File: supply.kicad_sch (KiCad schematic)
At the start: 166 parts, among them IC1 TPS54561, J3 DC_SOCKET, J8 61300311121, U10 LM3881MME_NOPB, U12 AP62301WU-7, U17 SN74LVC1G125DBVR, U18 MAX812REUS+T, U19 PAC1954T-E/4MX, U2 TPS65295RJET, U20 PAC1954T-E/4MX, U21 SN74LVC1G125DBVR, U22 SN74LVC1G125DBVR, U23 SN74LVC1G125DBVR, U4 AP62301WU-7, U5 AP62301WU-7, U9 AP62301WU-7

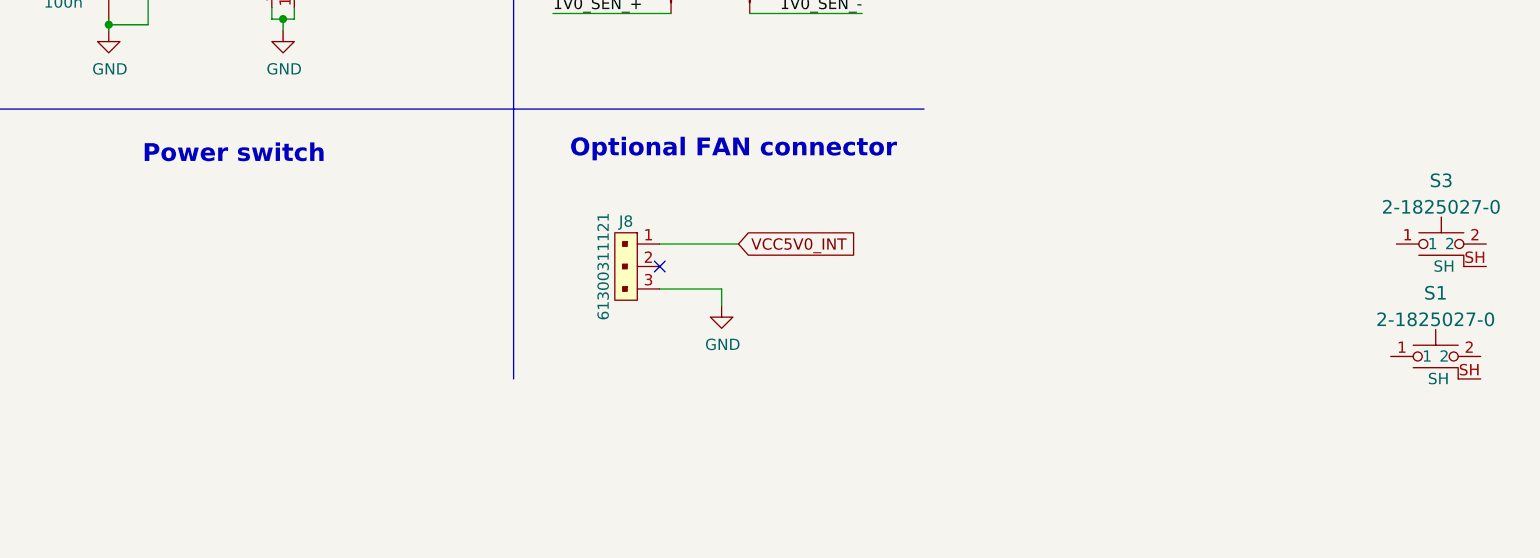
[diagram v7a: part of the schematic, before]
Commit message: Improve mechanical concept
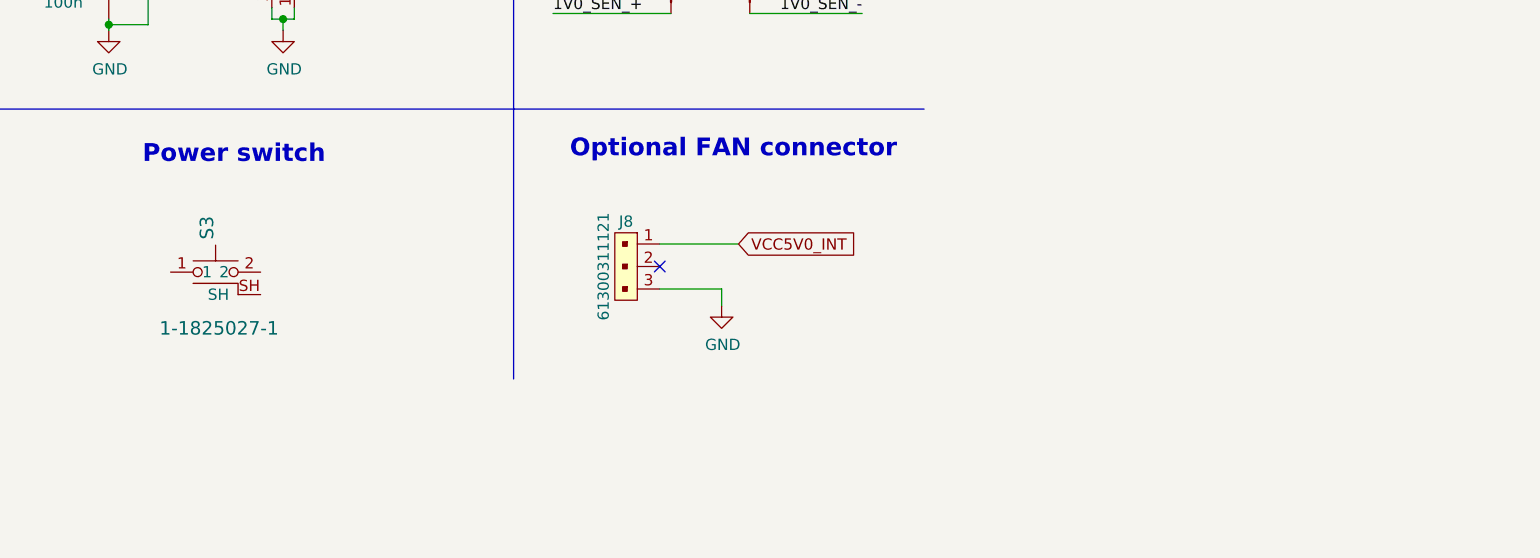
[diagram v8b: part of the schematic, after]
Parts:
- removed S1, S3: 2-1825027-0, antmicro-footprints:TE_2-1825027-0, symbol antmicroTactileSwitches:2-1825027-0
- added S3: 1-1825027-1, antmicro-footprints:TE_1-1825027-1, symbol antmicroTactileSwitches:1-1825027-1
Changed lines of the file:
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@@
     (pin "2")
+  )
+  (symbol (lib_id "antmicroTactileSwitches:1-1825027-1") (at 327.66 239.395 0) (unit 1)
+    (in_bom yes) (on_board yes)
+    (property "Reference" "S3" (id 0) (at 326.6838 236.982 90)
+      (effects (font (size 1.524 1.524)) (justify left))
+    )
+    (property "Value" "1-1825027-1" (id 1) (at 321.31 247.015 0)
+      (effects (font (size 1.524 1.524)) (justify left))
+    )
+    (property "Footprint" "antmicro-footprints:TE_1-1825027-1" (id 2) (at 332.74 234.315 0)
+      (effects (font (size 1.524 1.524)) (justify left) hide)
+    )
+    (property "Datasheet" "https://www.te.com/commerce/DocumentDelivery/DDEController?Action=showdoc&DocId=Customer+Drawing%7F1825027%7FH1%7Fpdf%7FEnglish%7FENG_CD_1825027_H1.pdf%7F1-1825027-1" (id 3) (at 332.74 231.775 0)
+      (effects (font (size 1.524 1.524)) (justify left) hide)
+    )
+    (property "MPN" "1-1825027-1" (id 4) (at 332.74 226.695 0)
+      (effects (font (size 1.524 1.524)) (justify left) hide)
+    )
+    (property "Manufacturer" "TE Connectivity" (id 5) (at 332.74 211.455 0)
+      (effects (font (size 1.524 1.524)) (justify left) hide)
+    )
+    (pin "1")
+    (pin "2")
+    (pin "SH")
   )
   (symbol (lib_id "antmicroResistorsmisc:R_0R01_1206") (at 383.54 127.635 0) (unit 1)
@@
     (pin "2")
   )
-  (symbol (lib_id "antmicroTactileSwitches:2-1825027-0") (at 465.455 248.92 0) (unit 1)
-    (in_bom yes) (on_board yes) (fields_autoplaced)
-    (property "Reference" "S1" (id 0) (at 465.455 243.0579 0)
-      (effects (font (size 1.524 1.524)))
-    )
-    (property "Value" "2-1825027-0" (id 1) (at 465.455 246.0513 0)
-      (effects (font (size 1.524 1.524)))
-    )
-    (property "Footprint" "antmicro-footprints:TE_2-1825027-0" (id 2) (at 470.535 243.84 0)
-      (effects (font (size 1.524 1.524)) (justify left) hide)
-    )
-    (property "Datasheet" "https://www.te.com/commerce/DocumentDelivery/DDEController?Action=showdoc&DocId=Customer+Drawing%7F1825027%7FH1%7Fpdf%7FEnglish%7FENG_CD_1825027_H1.pdf%7F2-1825027-0" (id 3) (at 470.535 241.3 0)
-      (effects (font (size 1.524 1.524)) (justify left) hide)
-    )
-    (property "MPN" "2-1825027-0" (id 4) (at 470.535 236.22 0)
-      (effects (font (size 1.524 1.524)) (justify left) hide)
-    )
-    (property "Manufacturer" "TE Connectivity" (id 5) (at 470.535 220.98 0)
-      (effects (font (size 1.524 1.524)) (justify left) hide)
-    )
-    (pin "1")
-    (pin "2")
-    (pin "SH")
-  )
   (symbol (lib_id "antmicroPMICPowerSequencers:MAX812REUS+T") (at 232.41 35.56 0) (unit 1)
     (in_bom yes) (on_board yes) (fields_autoplaced)
@@
     (pin "4")
   )
-  (symbol (lib_id "antmicroTactileSwitches:2-1825027-0") (at 466.09 236.22 0) (unit 1)
-    (in_bom yes) (on_board yes) (fields_autoplaced)
-    (property "Reference" "S3" (id 0) (at 466.09 230.3579 0)
-      (effects (font (size 1.524 1.524)))
-    )
-    (property "Value" "2-1825027-0" (id 1) (at 466.09 233.3513 0)
-      (effects (font (size 1.524 1.524)))
-    )
-    (property "Footprint" "antmicro-footprints:TE_2-1825027-0" (id 2) (at 471.17 231.14 0)
-      (effects (font (size 1.524 1.524)) (justify left) hide)
-    )
-    (property "Datasheet" "https://www.te.com/commerce/DocumentDelivery/DDEController?Action=showdoc&DocId=Customer+Drawing%7F1825027%7FH1%7Fpdf%7FEnglish%7FENG_CD_1825027_H1.pdf%7F2-1825027-0" (id 3) (at 471.17 228.6 0)
-      (effects (font (size 1.524 1.524)) (justify left) hide)
-    )
-    (property "MPN" "2-1825027-0" (id 4) (at 471.17 223.52 0)
-      (effects (font (size 1.524 1.524)) (justify left) hide)
-    )
-    (property "Manufacturer" "TE Connectivity" (id 5) (at 471.17 208.28 0)
-      (effects (font (size 1.524 1.524)) (justify left) hide)
-    )
-    (pin "1")
-    (pin "2")
-    (pin "SH")
-  )
   (symbol (lib_id "antmicroResistorsmisc:R_0R005_1206") (at 382.905 136.525 0) (unit 1)
